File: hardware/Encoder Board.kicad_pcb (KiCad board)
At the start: 2 copper layers, 32.5 x 32.5 mm, 24 parts, among them J1 Conn_01x08_Female, SW1 Rotary_Encoder_Switch

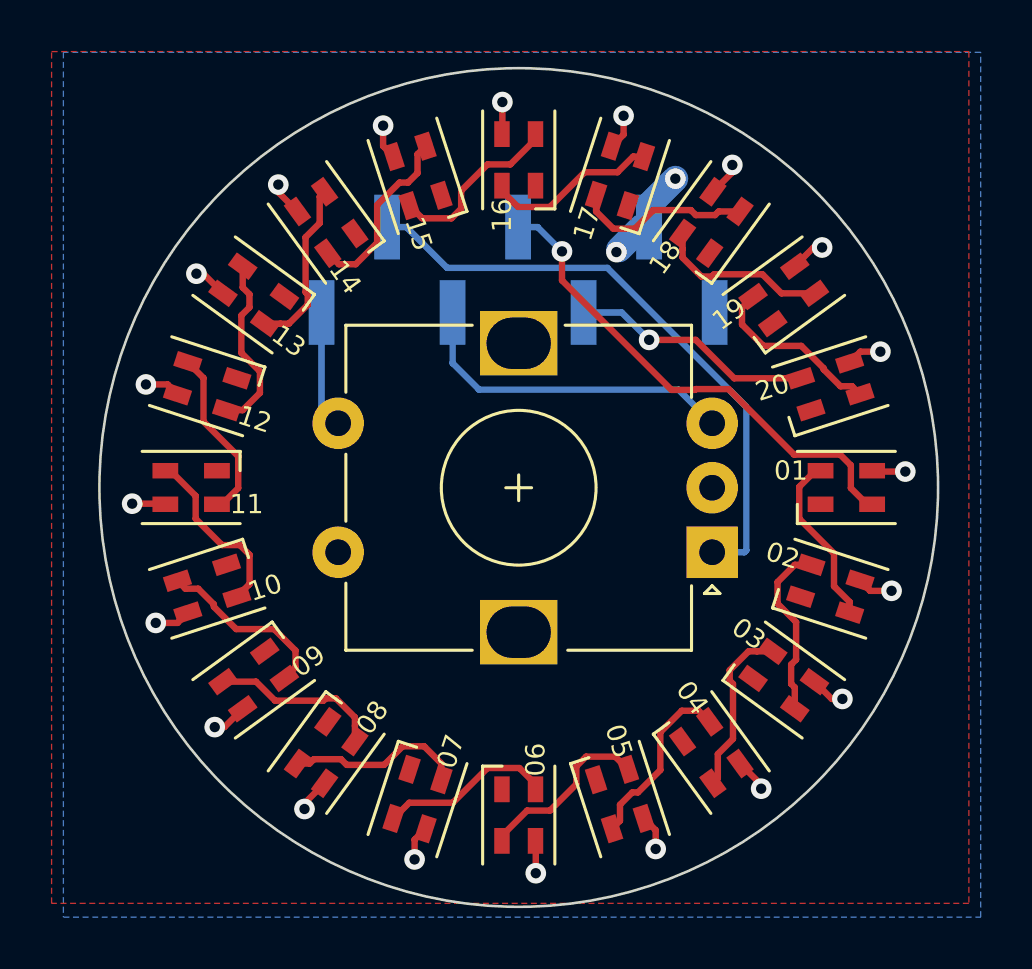
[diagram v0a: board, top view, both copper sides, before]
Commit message: First commit of v2, supporting RGB Encoders
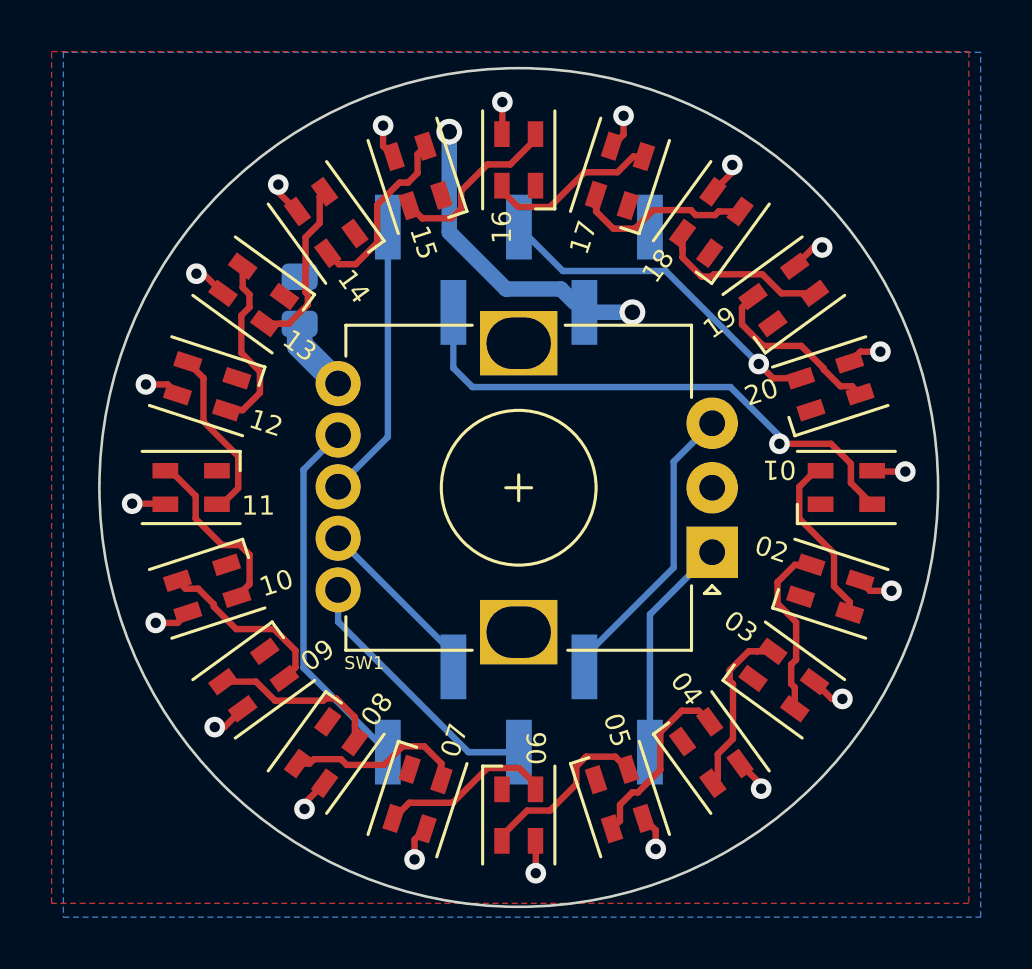
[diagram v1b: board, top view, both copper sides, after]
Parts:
- removed the G*** at (179.0, 77.0)
- added G***: LOGO, Andys-Footprints:Yoshi-Egg-Small, B.Cu at (168.1, 83.3)
- added J2: Conn_01x06_Male, Connector_PinHeader_2.54mm:PinHeader_1x05_P2.54mm_Vertical_SMD_Pin1Left, B.Cu at (179.0, 85.5)
- added R1: 200R, Resistor_SMD:R_0805_2012Metric, B.Cu at (170.5, 69.6)
- J1: value Conn_01x08_Female -> Conn_01x04_Male; footprint Connector_PinHeader_2.54mm:PinHeader_1x07_P2.54mm_Vertical_SMD_Pin1Left -> Connector_PinHeader_2.54mm:PinHeader_1x05_P2.54mm_Vertical_SMD_Pin1Right
- SW1: footprint Rotary_Encoder:RotaryEncoder_Alps_EC12E-Switch_Vertical_H20mm -> Andys-Footprints:LED_RotaryEncoder_Alps_EC12E-Switch_Vertical_H20mm
- moved G*** 0.91 mm to (179.0, 76.9)
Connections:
- J1 pad 5: ENC_B -> SW_A
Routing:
- net ENC_A: track 23.7 -> 8.75 mm
- net T2 / Blue: track 0.00 -> 14.2 mm
- net T5 / Red: track 0.00 -> 10.3 mm
- net GND: track 3.82 -> 12.3 mm
- net T4 / Green: track 0.00 -> 6.83 mm
- net SW_A: track 4.56 -> 10.9 mm
- net DOUT: track 9.47 -> 13.3 mm
- net Net-(R1-Pad2): track 0.00 -> 2.93 mm
- net DIN: track 19.4 -> 21.4 mm
- net ENC_B: track 13.0 -> 11.5 mm
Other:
- net class Default removed
- board text added: "Original design by Adam Zeloof v2 by Andy Hofmann"
- board text added: "Power, LEDs & Switch"
- board text added: "Rotary Encoder"
- board text added: "engineering"
- board text added: "isotope"
- board text added: "v2.0"
